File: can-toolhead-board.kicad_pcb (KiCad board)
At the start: 4 copper layers, 51 x 36.9 mm, 95 parts, among them J1 MF3-2x2P, J10 PH-2P, J11 PH-2P, J12 PH-2P, J13 PH-2P, J14 PH-2P, J15 PH-3P, J2 USB_C_Receptacle_USB2.0, J3 SH-6P, J4 PH-2P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

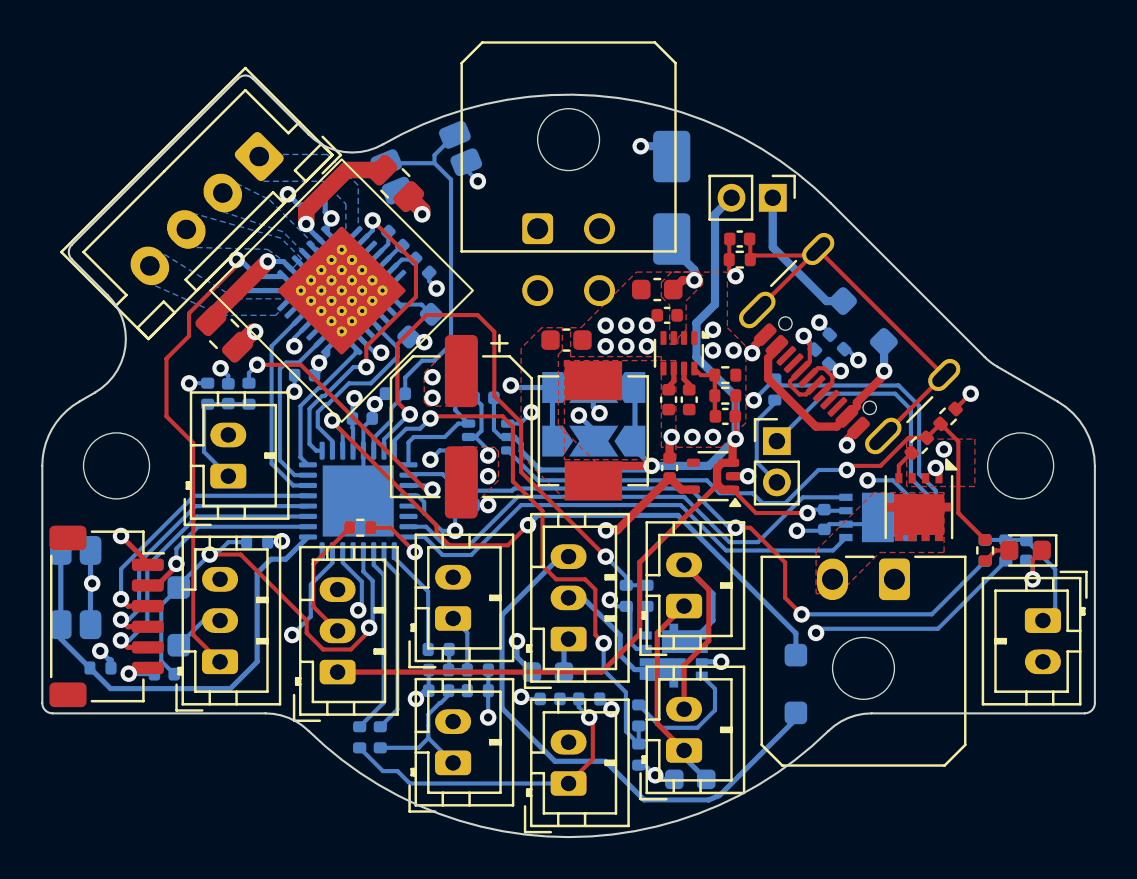
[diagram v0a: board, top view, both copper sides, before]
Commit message: Added solder jumpers for CAN/USB interface selection
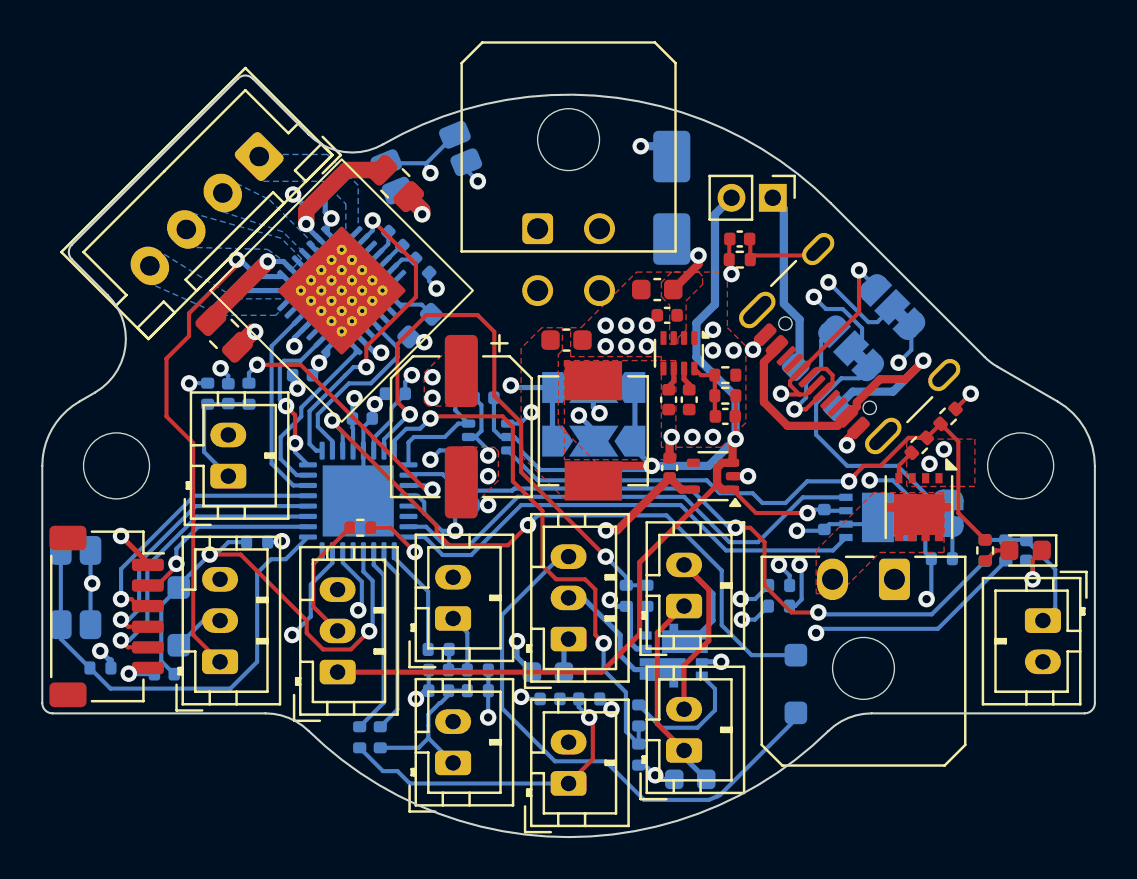
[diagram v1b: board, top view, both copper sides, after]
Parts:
- added JP5: SolderJumper_3_Bridged12, Jumper:SolderJumper-3_P1.3mm_Bridged12_RoundedPad1.0x1.5mm, B.Cu at (115.7, 92.3)
- added JP6: SolderJumper_3_Bridged12, Jumper:SolderJumper-3_P1.3mm_Bridged12_RoundedPad1.0x1.5mm, B.Cu at (113.7, 94.3)
- JP1: footprint Connector_PinHeader_2.00mm:PinHeader_1x02_P2.00mm_Vertical -> Jumper:SolderJumper-2_P1.3mm_Bridged_RoundedPad1.0x1.5mm; moved to B.Cu
- moved R6 13.0 mm to (110.2, 106.8), turned to 0 degrees
- moved R1 11.5 mm to (118.1, 104.5), turned to 0 degrees
- moved R5 11.4 mm to (110.2, 105.8), turned to 0 degrees
- moved JP1 9.01 mm to (118.4, 102.3), turned to -90 degrees
- moved D2 3.94 mm to (112.0, 96.2)
- moved C20 0.10 mm to (87.1, 95.6)
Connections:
- J1 pad 3: CANH -> /D+
- J1 pad 4: CANL -> /D-
- J2 pad A6: Net-(J2-D+-PadA6) -> USB_D+
- J2 pad A7: Net-(J2-D--PadA7) -> USB_D-
- J2 pad B6: Net-(J2-D+-PadA6) -> USB_D+
- J2 pad B7: Net-(J2-D--PadA7) -> USB_D-
- R5 pad 1: Net-(J2-D--PadA7) -> Net-(U4-PA11/PA9)
- R5 pad 2: /MCU/USB_D+ -> USB_D-
- R6 pad 1: Net-(J2-D+-PadA6) -> Net-(U4-PA12/PA10)
- R6 pad 2: /MCU/USB_D- -> USB_D+
- U4 pad 22: /MCU/USB_D- -> Net-(U4-PA11/PA9)
- U4 pad 23: /MCU/USB_D+ -> Net-(U4-PA12/PA10)
- U4 pad 31: MOT_STEP -> MOT_UART
- U4 pad 32: MOT_UART -> MOT_STEP
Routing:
- net /MCU/USB_D+: track 43.7 -> 0.00 mm, vias 2 -> 0
- net /MCU/USB_D-: track 39.9 -> 0.00 mm, vias 2 -> 0
- net Net-(U4-PA12/PA10): track 0.00 -> 29.9 mm, vias 0 -> 2
- net Net-(U4-PA11/PA9): track 0.00 -> 25.7 mm, vias 0 -> 2
- net USB_D+: track 0.00 -> 24.8 mm, vias 0 -> 3
- net /D+: track 0.00 -> 19.5 mm, vias 0 -> 1
- net USB_D-: track 0.00 -> 19.3 mm, vias 0 -> 2
- net /D-: track 0.00 -> 15.1 mm, vias 0 -> 1
- net /MCU/~{RST}: track 20.3 -> 33.9 mm, vias 0 -> 2
- net CANL: track 25.5 -> 13.8 mm
- net CANH: track 29.6 -> 19.9 mm, vias 1 -> 2
- net Net-(D2-A): track 11.1 -> 17.8 mm
- net Net-(J2-D+-PadA6): track 5.40 -> 0.00 mm, vias 1 -> 0
- net Net-(J2-D--PadA7): track 3.70 -> 0.00 mm, vias 1 -> 0
- net Net-(JP1-B): track 4.76 -> 1.64 mm
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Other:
- board text added: "CAN"
- board text added: "CTB v1.0-9999999"
- board text added: "G"
- board text added: "USB"

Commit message: Layout tweaks/pinout optimization
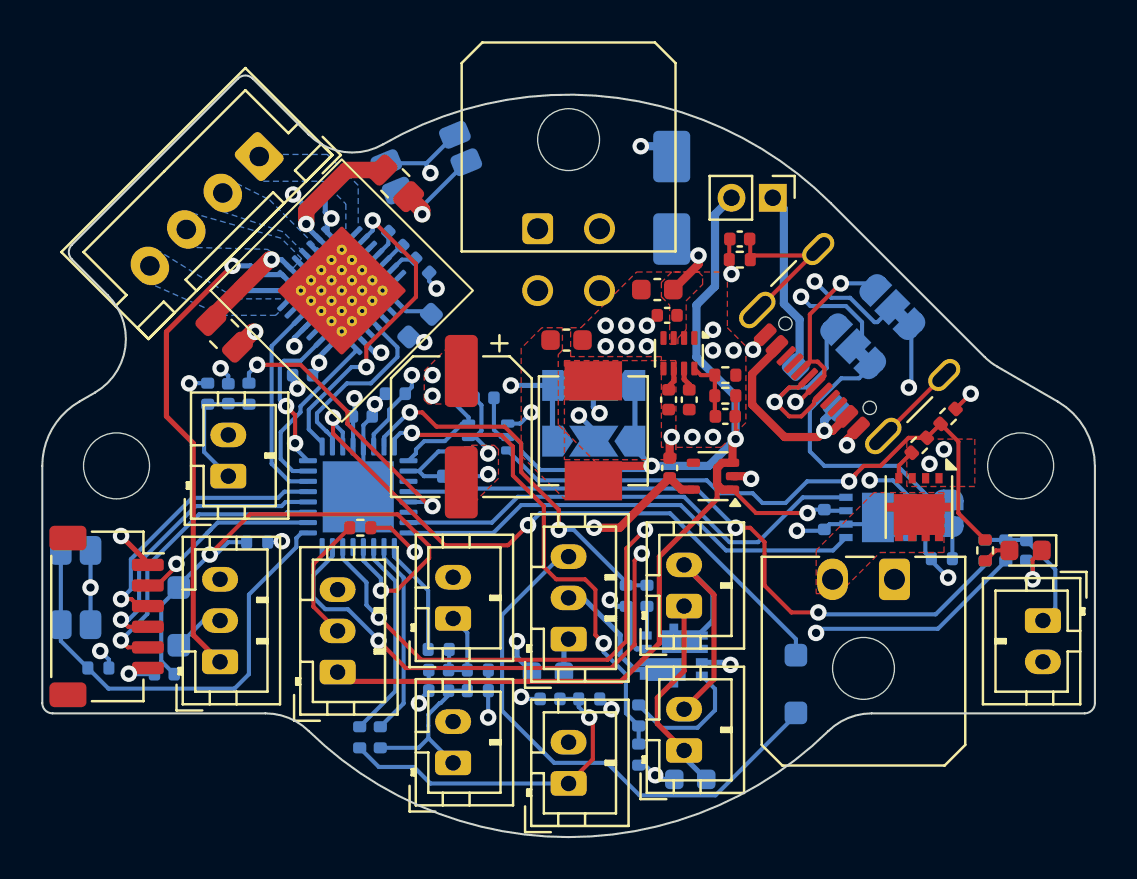
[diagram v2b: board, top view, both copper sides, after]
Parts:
- removed R5, R6: 27R, Resistor_SMD:R_0402_1005Metric
- moved R8 1.49 mm to (94.4, 100.5)
- moved U4 0.20 mm to (89.8, 101.5)
- moved C19 0.14 mm to (84.5, 90.9)
- moved JP6 0.14 mm to (113.8, 94.2)
- moved C12 0.10 mm to (90.0, 97.6)
- moved JP3 0.10 mm to (101.2, 96.1)
- moved R7 0.10 mm to (77.2, 109.8)
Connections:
- U4 pad 10: TH0 -> HE
- U4 pad 11: TH1 -> unconnected-(U4-PA4-Pad11)
- U4 pad 12: HE -> TH0
- U4 pad 13: unconnected-(U4-PA6-Pad13) -> TH1
- U4 pad 22: Net-(U4-PA11/PA9) -> USB_D-
- U4 pad 23: Net-(U4-PA12/PA10) -> USB_D+
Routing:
- net Net-(U4-PA12/PA10): track 29.9 -> 0.00 mm, vias 2 -> 0
- net Net-(U4-PA11/PA9): track 25.7 -> 0.00 mm, vias 2 -> 0
- net USB_D-: track 19.3 -> 43.2 mm, vias 2 -> 3
- net USB_D+: track 24.8 -> 45.5 mm, vias 3 -> 4
- net FAN0: track 27.5 -> 18.6 mm
- net Net-(D2-A): track 17.8 -> 10.3 mm
- net HE: track 10.6 -> 4.58 mm, vias 2 -> 0
- net PROBE: track 23.6 -> 27.2 mm
- net GND: track 62.4 -> 65.5 mm, vias 42 -> 40
- net CANH: track 19.9 -> 17.3 mm
- net FAN1: track 26.5 -> 24.3 mm
- net +5V: track 71.5 -> 72.8 mm
- net CANL: track 13.8 -> 14.9 mm
- net /MCU/CAN_RX: track 24.4 -> 23.5 mm
- net FAN1_SENSE: track 31.9 -> 31.0 mm
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
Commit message: Change 3V3 output cap to 4u7
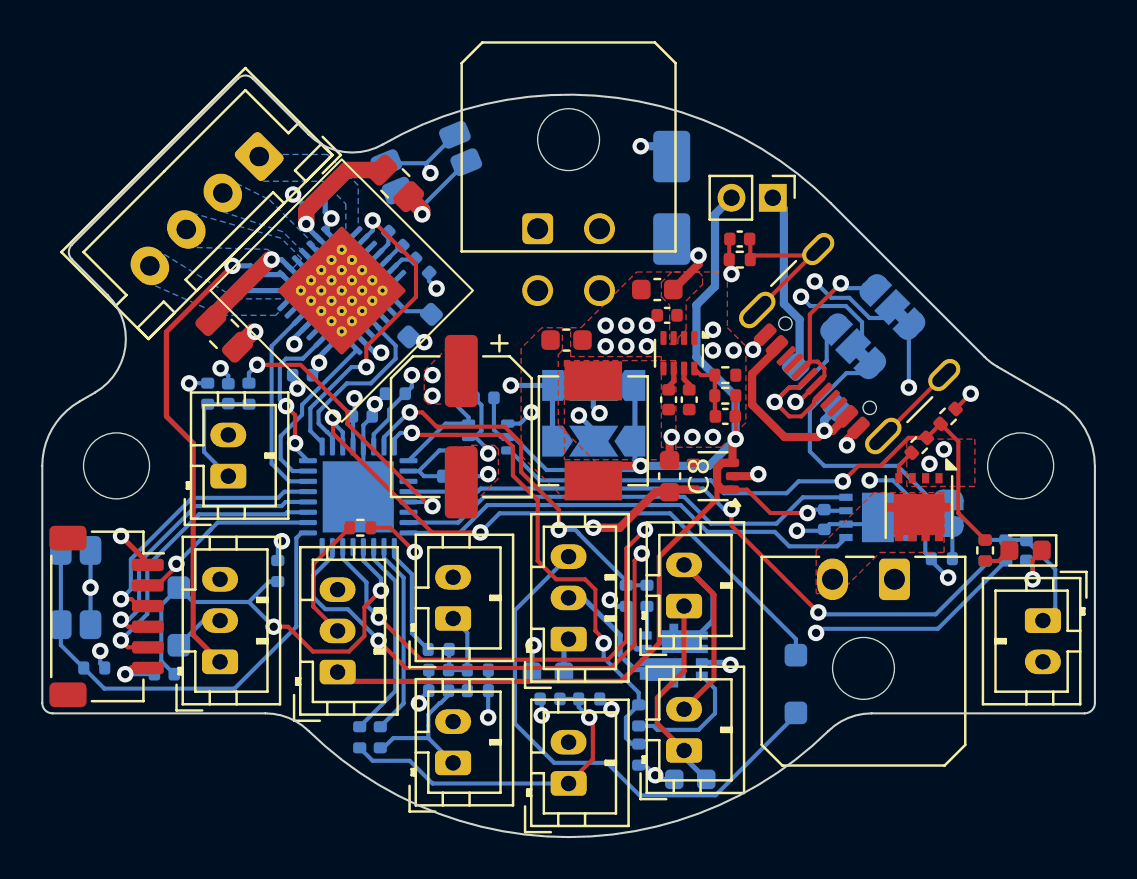
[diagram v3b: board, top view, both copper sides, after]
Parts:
- C8: value 1u -> 4u7; footprint Capacitor_SMD:C_0402_1005Metric -> Capacitor_SMD:C_0603_1608Metric
- moved R30 1.72 mm to (85.9, 105.1), turned to -90 degrees
- moved C8 0.40 mm to (104.9, 100.5)
- moved R7 0.20 mm to (77.0, 109.8)
- turned R12 to -90 degrees
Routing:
- net PROBE: track 27.2 -> 22.2 mm
- net +5V: track 72.8 -> 71.8 mm
- net TH0: track 33.0 -> 32.2 mm
- net Net-(D4-K): track 26.7 -> 26.0 mm
- net /MCU/CAN_RX: track 23.5 -> 22.8 mm
- net FAN1: track 24.3 -> 25.0 mm
- net FAN1_SENSE: track 31.0 -> 30.5 mm
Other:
- board text added: "PROBE"
- board text removed: "Probe"

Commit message: Rename fan ports to PCF/HEF
Remove USB series resistors

Add USB clamping diodes
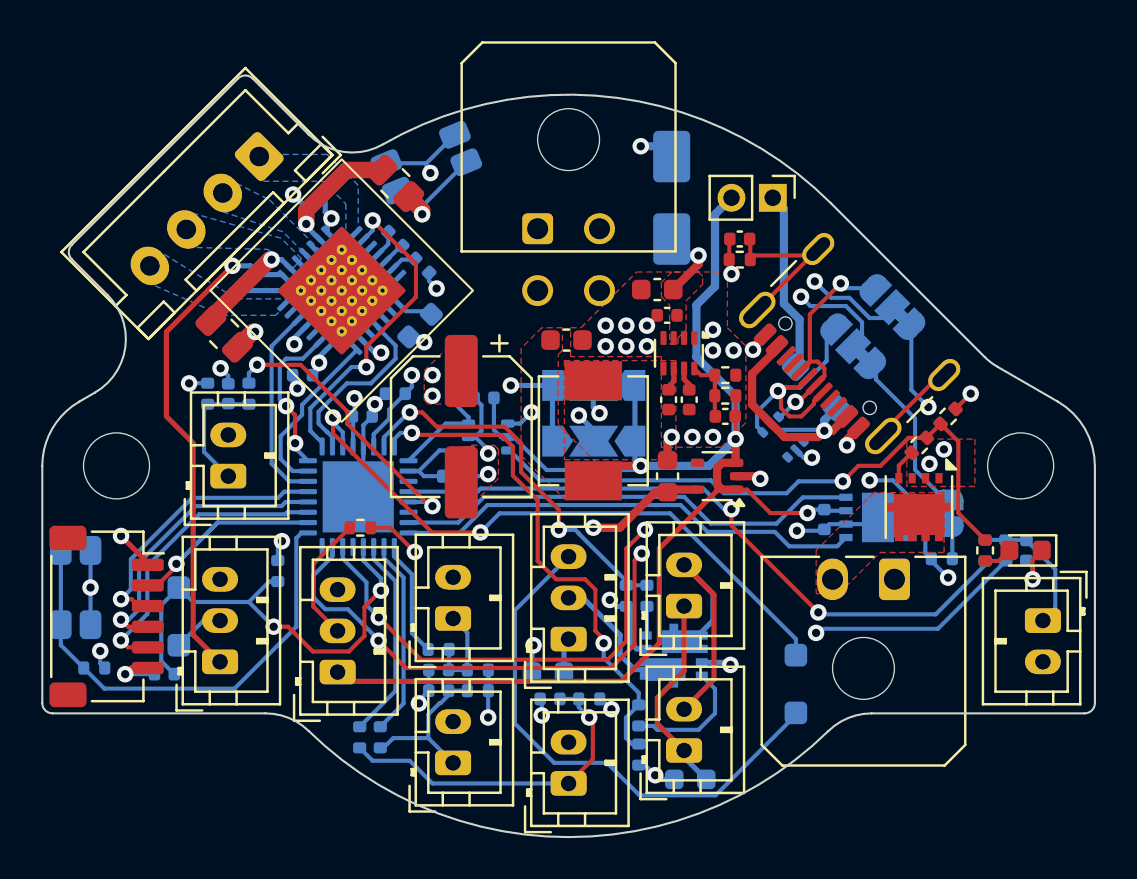
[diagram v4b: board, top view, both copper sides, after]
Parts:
- added U7: USBLC6-2P6, Package_TO_SOT_SMD:SOT-666, B.Cu at (110.4, 98.6)
- moved U2 0.20 mm to (107.2, 100.5)
- moved C8 0.10 mm to (104.8, 100.5)
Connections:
- net /Outputs/FAN0_PWR renamed /Outputs/PCFAN_PWR
- net /Outputs/FAN1_PWR renamed /Outputs/HEFAN_PWR
- net FAN0 renamed PCFAN
- net FAN1 renamed HEFAN
- net FAN1_SENSE renamed HEFAN_SENSE
- net Net-(D2-A) renamed VBUS
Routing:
- net CANL: track 14.9 -> 10.2 mm
- net USB_D-: track 43.0 -> 45.8 mm
- net VBUS: track 10.3 -> 13.1 mm
- net /MCU/~{SS}: track 9.36 -> 11.9 mm
- net USB_D+: track 45.5 -> 46.7 mm
- net GND: track 65.6 -> 66.4 mm, vias 40 -> 41
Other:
- board text added: "HEF"
- board text added: "PCF"
- board text removed: "F0"
- board text removed: "F1"

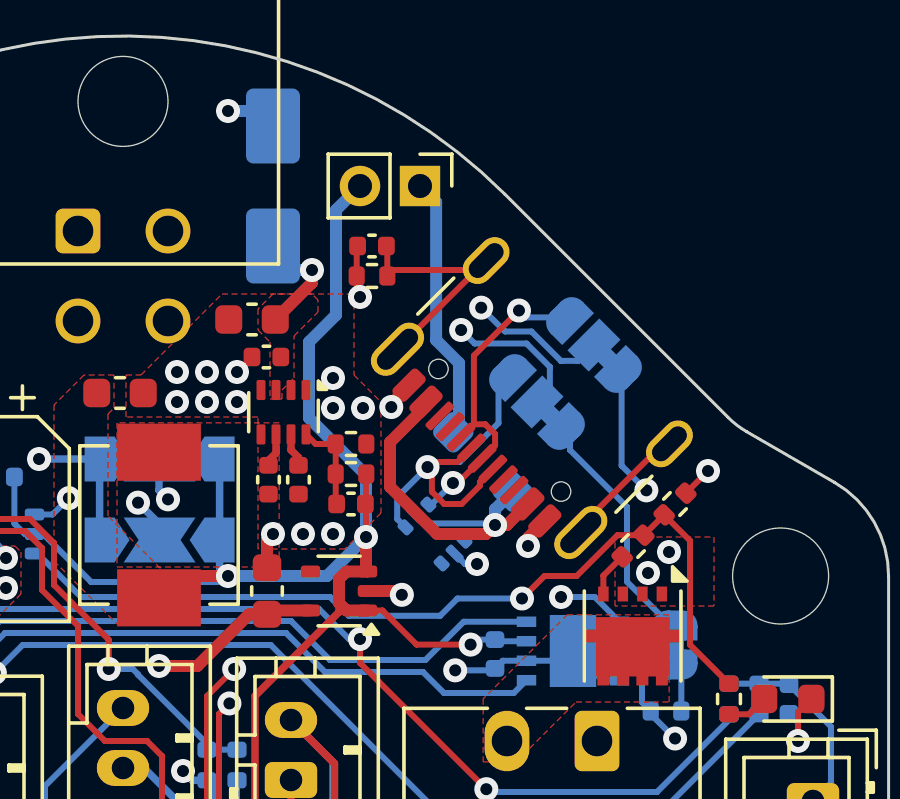
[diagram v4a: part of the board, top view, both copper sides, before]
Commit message: Add USB CC pulldown resistors
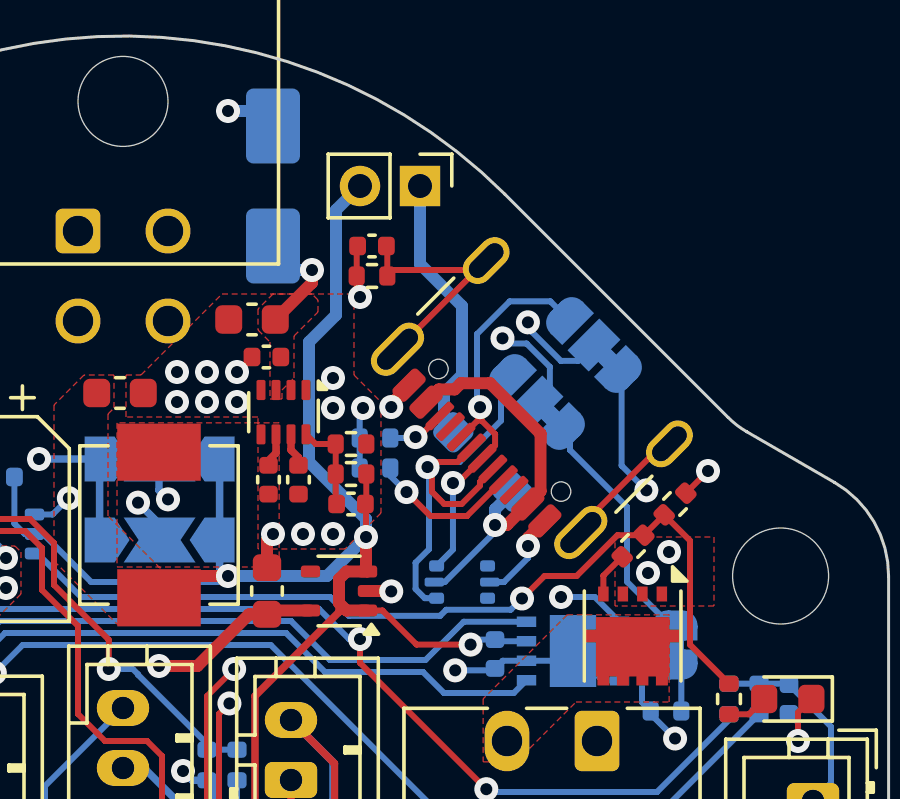
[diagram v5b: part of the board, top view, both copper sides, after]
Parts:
- added R5: 5K1, Resistor_SMD:R_0402_1005Metric, B.Cu at (108.4, 96.4)
- added R6: 5K1, Resistor_SMD:R_0402_1005Metric, B.Cu at (108.4, 95.4)
- moved U7 1.84 mm to (111.3, 100.2), turned to 180 degrees
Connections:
- net /MCU/BOOT0 renamed /BOOT0
- net /MCU/CAN_RX renamed /CAN_RX
- net /MCU/CAN_TX renamed /CAN_TX
- net /MCU/MISO renamed /MISO
- net /MCU/MOSI renamed /MOSI
- net /MCU/SCK renamed /SCK
- net /MCU/SWDIO renamed /SWDIO
- net /MCU/~{RST} renamed /~{RST}
- net /MCU/~{SS} renamed /~{SS}
- J2 pad A5: unconnected-(J2-CC1-PadA5) -> Net-(J2-CC1)
- J2 pad B5: unconnected-(J2-CC2-PadB5) -> Net-(J2-CC2)
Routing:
- net Net-(J2-CC1): track 0.00 -> 5.09 mm, vias 0 -> 1
- net GND: track 66.4 -> 69.2 mm, vias 41 -> 40
- net USB_D-: track 45.8 -> 48.4 mm
- net USB_D+: track 46.7 -> 49.1 mm
- net Net-(J2-CC2): track 0.00 -> 1.95 mm, vias 0 -> 1

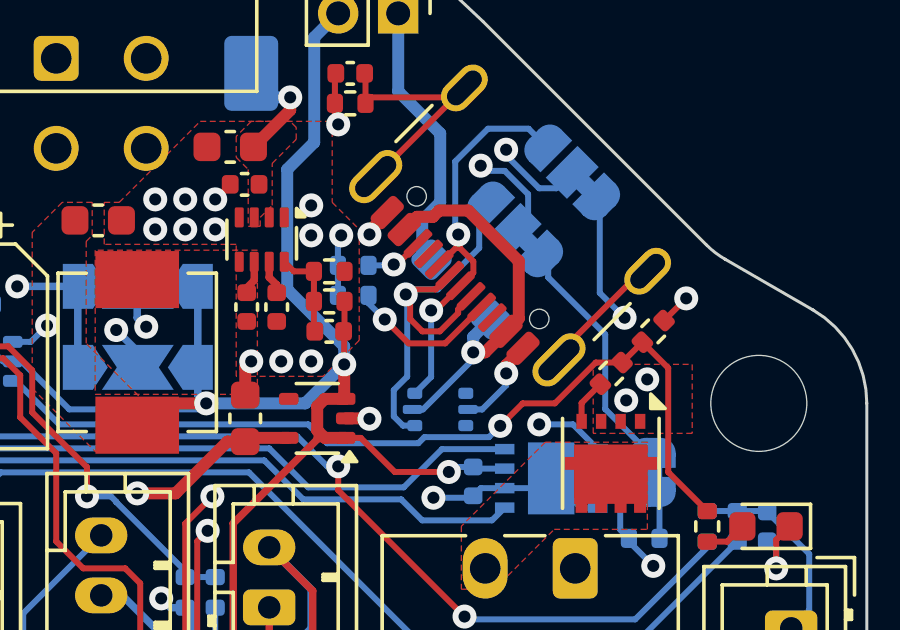
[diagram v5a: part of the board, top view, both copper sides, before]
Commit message: Add 3D models
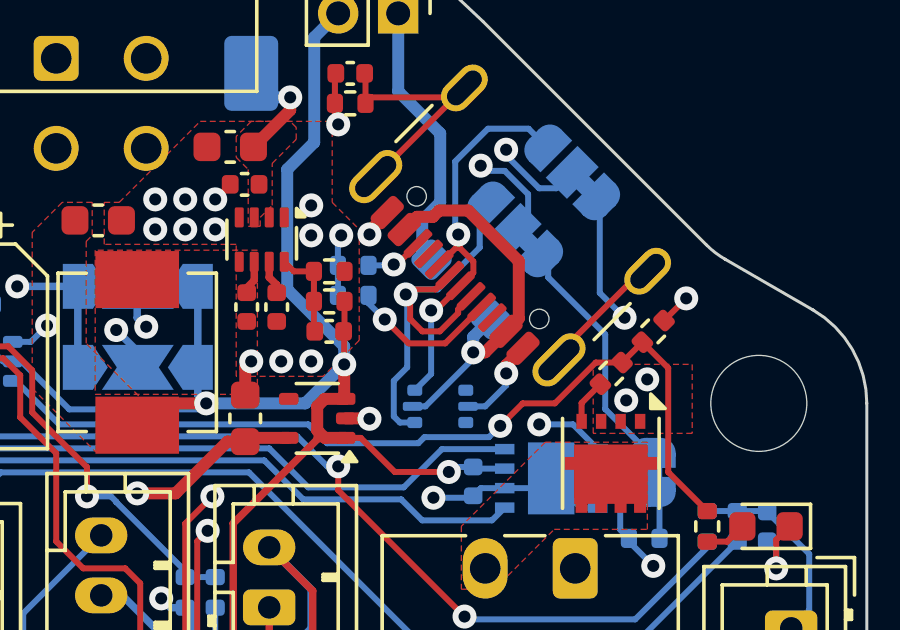
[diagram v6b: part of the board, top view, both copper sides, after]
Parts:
- moved U7 0.10 mm to (111.3, 100.1)
